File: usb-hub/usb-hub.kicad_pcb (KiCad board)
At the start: 2 copper layers, 32 x 43 mm, 58 parts, among them J5 USB_A, J7 USB_C_Receptacle, J8 USB_C_Receptacle, P1 CONN_01X04, P2 CONN_02X03, U1 usb-2412, U2 LD1117S12TR_SOT223, U3 rgbled, U4 ATmega32U4, U5 24LC16, Y1 Crystal_GND24, Y2 Crystal_GND24

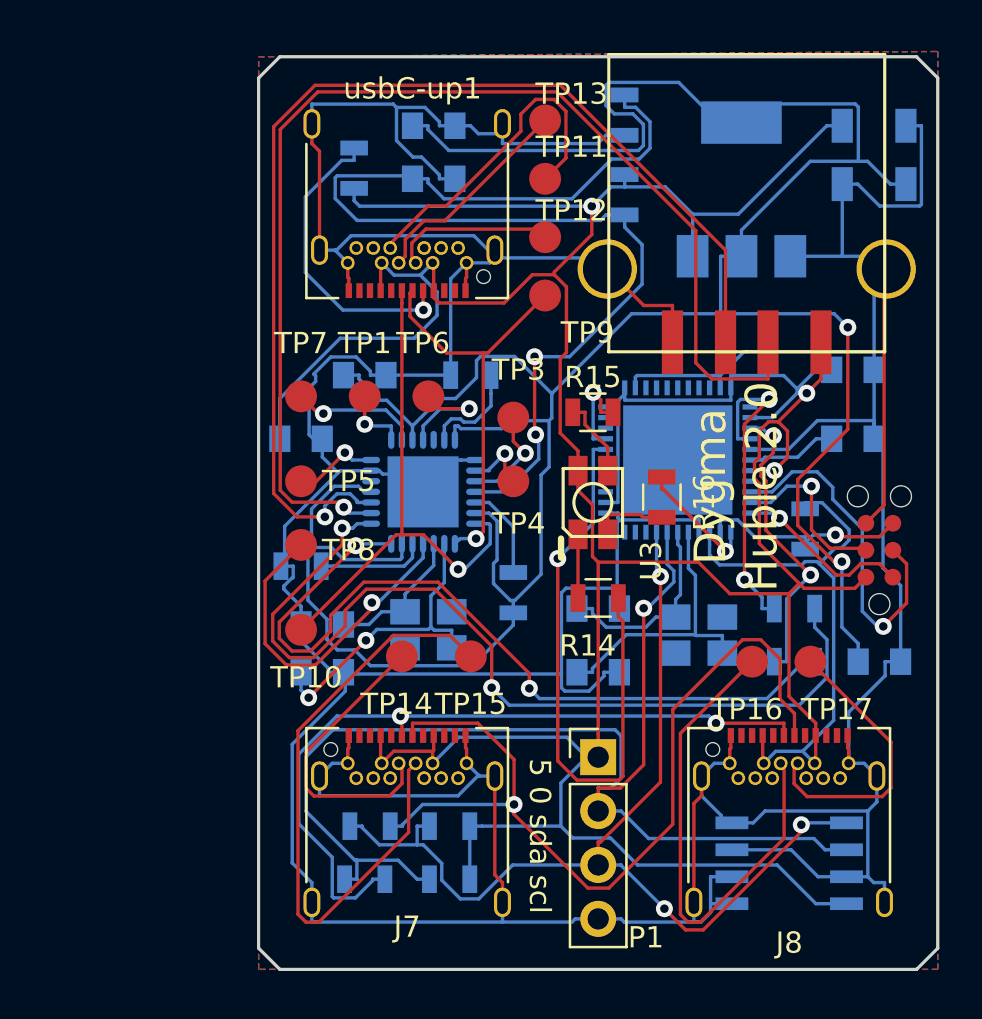
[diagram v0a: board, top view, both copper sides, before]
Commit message: fixed usb routing, added reset, bigger board, dygma logo
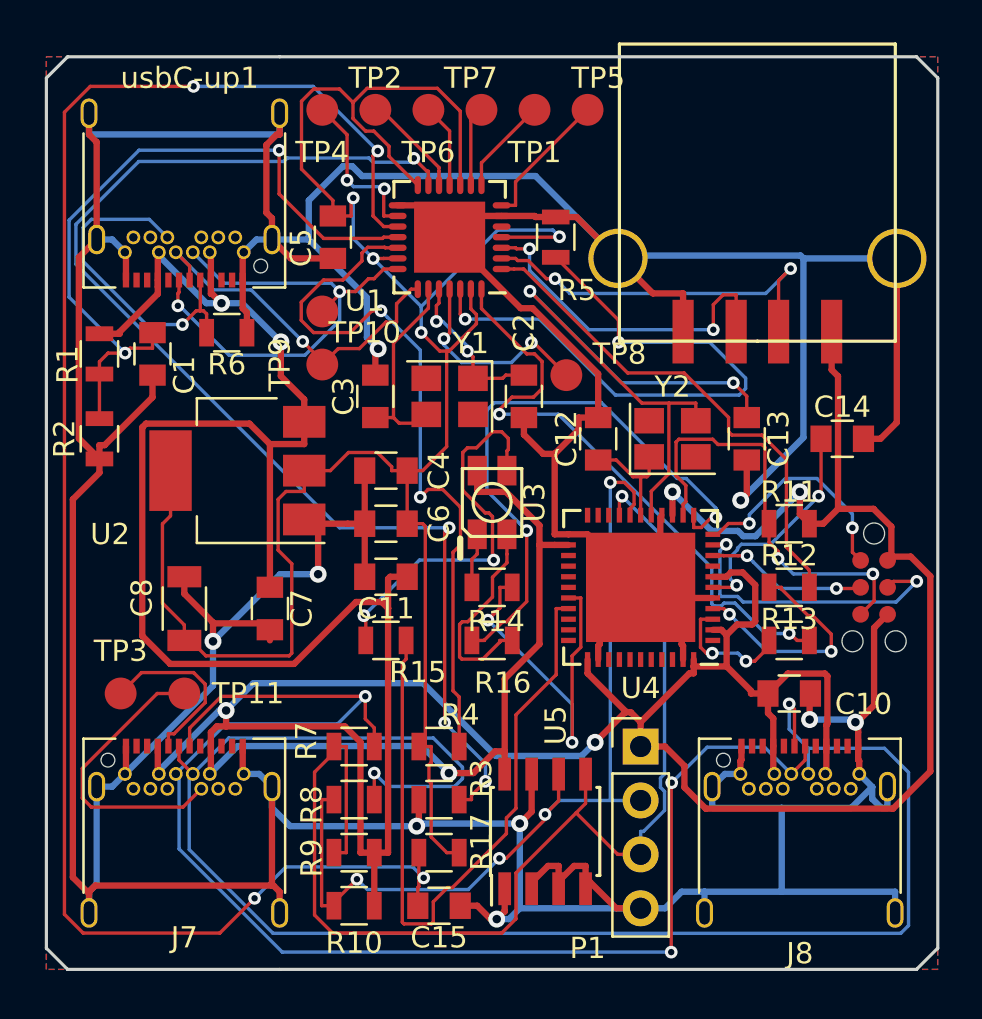
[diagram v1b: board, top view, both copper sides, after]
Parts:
- removed TP12, TP13, TP14, TP15, TP16, TP17: TEST, Measurement_Points:Measurement_Point_Round-SMD-Pad_Small
- added C15: 0.1u, Capacitors_SMD:C_0805, F.Cu at (127.5, 118.0)
- added R17: 10k, Resistors_SMD:R_0805, F.Cu at (127.5, 115.5)
- added TP2: TEST, Measurement_Points:Measurement_Point_Round-SMD-Pad_Small, F.Cu at (124.5, 80.5)
- added svg2mod: G***, fp:dygma-logo, B.Cu at (127.6, 99.6)
- C1, C11, C14, C2, C3, C4, C5, C6, R1, R10, R11, R12, R13, R2, R3, R4, R5, R7, R8, R9, U1, U2, U4, U5, Y1, Y2: moved to F.Cu
- C10: value 1u -> 4.7u; moved to F.Cu
- C12, C13: value 30pf -> 20pf; moved to F.Cu
- C7: value CP1 -> 0.1u; footprint Capacitors_SMD:C_1206 -> Capacitors_SMD:C_0805; moved to F.Cu
- C8: value CP1 -> 47u; moved to F.Cu
- R6: value 56k -> 5.1k; moved to F.Cu
- moved C8 38.2 mm to (115.5, 104.0), turned to 90 degrees
- moved C7 36.4 mm to (119.5, 104.0), turned to 270 degrees
- moved C5 32.6 mm to (122.5, 86.5), turned to 270 degrees
- moved TP11 29.6 mm to (115.5, 108.0)
- moved R2 29.1 mm to (111.5, 96.0)
- moved U2 27.2 mm to (118.0, 97.5), turned to 180 degrees
- moved R1 25.9 mm to (111.5, 92.0)
- moved TP3 22.6 mm to (112.5, 108.0)
- moved TP5 22.1 mm to (134.5, 80.5), turned to 270 degrees
- moved R3 20.1 mm to (127.5, 113.0)
- moved TP4 19.7 mm to (122.0, 80.5), turned to 90 degrees
- moved R5 19.6 mm to (133.0, 86.5), turned to 270 degrees
- moved C6 18.9 mm to (125.0, 100.0), turned to 180 degrees
- moved TP7 16.0 mm to (129.5, 80.5), turned to 270 degrees
- moved TP1 15.7 mm to (132.0, 80.5), turned to 270 degrees
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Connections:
- J7 pad B6: Net-(J7-PadB6) -> /huble/usbc-dp
- J7 pad B7: Net-(J7-PadB7) -> /huble/usbc-dn
- J8 pad B6: Net-(J8-PadB6) -> /huble/usbc-dp
- J8 pad B7: Net-(J8-PadB7) -> /huble/usbc-dn
- R6 pad 1: +5V -> Net-(R6-Pad1)
- R6 pad 2: Net-(R6-Pad2) -> Earth
- TP11 pad 1: Net-(TP11-Pad1) -> Net-(J7-PadB5)
- TP3 pad 1: Net-(TP3-Pad1) -> Net-(J7-PadA5)
- U1 pad 12: (no net) -> Net-(TP2-Pad1)
- U1 pad 17: Net-(TP3-Pad1) -> Net-(C15-Pad1)
- U4 pad 45: (no net) -> Earth
- usbC-up1 pad A5: Net-(R6-Pad2) -> Net-(R6-Pad1)
- usbC-up1 pad B5: Net-(TP11-Pad1) -> Net-(R6-Pad1)
- usbC-up1 pad B6: Net-(TP13-Pad1) -> /usb-up-p
- usbC-up1 pad B7: Net-(TP12-Pad1) -> /usb-up-n
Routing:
- net Net-(C15-Pad1): track 0.00 -> 80.4 mm, vias 0 -> 4
- net Earth: track 294.6 -> 352.0 mm, vias 0 -> 9
- net Net-(R3-Pad2): track 4.82 -> 58.1 mm, vias 0 -> 4
- net /huble/usbc-dp: track 35.5 -> 79.4 mm
- net /ext-usb-n: track 56.4 -> 18.0 mm, vias 1 -> 2
- net /ext-usb-p: track 52.9 -> 16.3 mm, vias 1 -> 2
- net +3V3: track 142.6 -> 107.3 mm, vias 2 -> 4
- net +5V: track 208.5 -> 238.9 mm, vias 3 -> 7
- net Net-(R4-Pad2): track 4.43 -> 34.6 mm, vias 0 -> 2
- net Net-(J7-PadB6): track 29.6 -> 0.00 mm
- net /huble/pwm_g: track 4.44 -> 32.8 mm, vias 1 -> 0
- net /huble/usbc-dn: track 41.2 -> 67.9 mm, vias 1 -> 3
- net Net-(R5-Pad2): track 5.12 -> 28.7 mm, vias 0 -> 2
- net Net-(J8-PadB7): track 23.6 -> 0.00 mm
- net /huble/pwm_b: track 5.79 -> 28.4 mm, vias 1 -> 2
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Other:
- board size 32 x 43 mm -> 42 x 43 mm
- net class Default: via_dia 0.8 -> 0.6; via_drill 0.4 -> 0.3
- net class power added: clearance 0.15, trace_width 0.3, via_dia 0.8, via_drill 0.4
- board text added: "$ver$ "8c3a289" 2018-01-18"
- board text added: "Huble 2.0"
- board text removed: "Dygma Huble 2.0"
